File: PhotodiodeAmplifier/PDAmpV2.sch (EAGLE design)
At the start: 21 parts, among them IC1 CA3140N, IC2 7812L

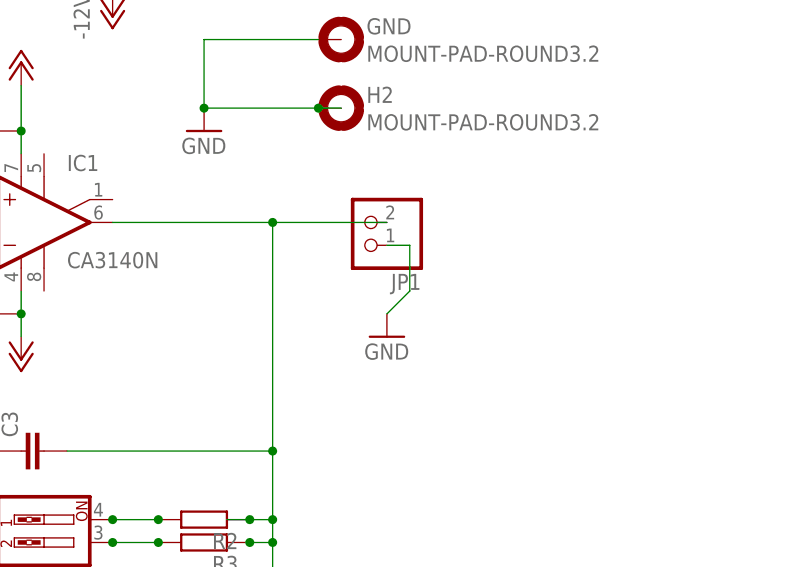
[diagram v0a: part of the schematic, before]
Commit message: Insert 50 ohm resistor into output
This actually makes the circuit work properly, previously I was doing this
with a terminator, but that's a bit dangerous for your ICS
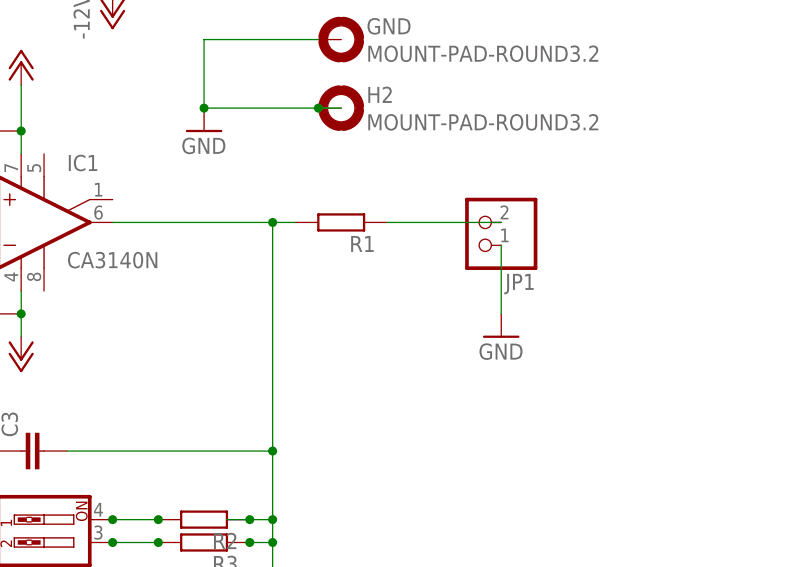
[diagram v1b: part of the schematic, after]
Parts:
- added R1: (no value), resistor:R-EU_0207/10
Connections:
- new net N$10: JP1.2, R1.1
- net N$16: now also R1.2; no longer JP1.2
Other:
- moved on the sheet: JP1
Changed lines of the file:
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@@
 <part name="R4" library="resistor" deviceset="R-EU_" device="0207/10"/>
 <part name="R5" library="resistor" deviceset="R-EU_" device="0207/10"/>
+<part name="R1" library="resistor" deviceset="R-EU_" device="0207/10"/>
 </parts>
 <sheets>
@@
 </plain>
 <instances>
-<instance part="JP1" gate="G$1" x="111.76" y="58.42" rot="R180"/>
+<instance part="JP1" gate="G$1" x="124.46" y="58.42" rot="R180"/>
 <instance part="GND1" gate="1" x="83.82" y="93.98"/>
 <instance part="GND2" gate="1" x="93.98" y="68.58"/>
@@
 <instance part="P-2" gate="1" x="73.66" y="43.18"/>
 <instance part="P+2" gate="1" x="73.66" y="76.2"/>
-<instance part="GND5" gate="1" x="114.3" y="45.72"/>
+<instance part="GND5" gate="1" x="127" y="45.72"/>
 <instance part="S1" gate="G$1" x="76.2" y="22.86" rot="R180"/>
 <instance part="S2" gate="G$1" x="76.2" y="12.7" rot="R180"/>
@@
 <instance part="R4" gate="G$1" x="93.98" y="15.24" rot="R180"/>
 <instance part="R5" gate="G$1" x="93.98" y="12.7" rot="R180"/>
+<instance part="R1" gate="G$1" x="109.22" y="58.42" rot="R180"/>
 </instances>
 <busses>
@@
 <pinref part="GND5" gate="1" pin="GND"/>
 <pinref part="JP1" gate="G$1" pin="1"/>
-<wire x1="114.3" y1="55.88" x2="116.84" y2="55.88" width="0.1524" layer="91"/>
-<wire x1="116.84" y1="55.88" x2="116.84" y2="50.8" width="0.1524" layer="91"/>
-<wire x1="116.84" y1="50.8" x2="114.3" y2="48.26" width="0.1524" layer="91"/>
+<wire x1="127" y1="55.88" x2="127" y2="48.26" width="0.1524" layer="91"/>
 </segment>
 </net>
@@
 <wire x1="101.6" y1="22.86" x2="99.06" y2="22.86" width="0.1524" layer="91"/>
 <pinref part="IC1" gate="A" pin="OUT"/>
-<pinref part="JP1" gate="G$1" pin="2"/>
 <wire x1="83.82" y1="58.42" x2="101.6" y2="58.42" width="0.1524" layer="91"/>
 <pinref part="C3" gate="G$1" pin="2"/>
-<wire x1="101.6" y1="58.42" x2="114.3" y2="58.42" width="0.1524" layer="91"/>
 <wire x1="78.74" y1="33.02" x2="101.6" y2="33.02" width="0.1524" layer="91"/>
 <wire x1="101.6" y1="33.02" x2="101.6" y2="58.42" width="0.1524" layer="91"/>
-<junction x="101.6" y="58.42"/>
 <wire x1="101.6" y1="33.02" x2="101.6" y2="25.4" width="0.1524" layer="91"/>
 <junction x="101.6" y="33.02"/>
@@
 <junction x="99.06" y="15.24"/>
 <junction x="99.06" y="12.7"/>
-</segment>
-</net>
+<pinref part="R1" gate="G$1" pin="2"/>
+<wire x1="104.14" y1="58.42" x2="101.6" y2="58.42" width="0.1524" layer="91"/>
+<junction x="101.6" y="58.42"/>
+</segment>
+</net>
+<net name="N$10" class="0">
+<segment>
+<pinref part="JP1" gate="G$1" pin="2"/>
+<pinref part="R1" gate="G$1" pin="1"/>
+<wire x1="127" y1="58.42" x2="114.3" y2="58.42" width="0.1524" layer="91"/>
+</segment>
+</net>
